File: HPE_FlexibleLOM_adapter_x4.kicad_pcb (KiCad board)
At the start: 4 copper layers, 79.2 x 21.7 mm, 8 parts, among them J1 Connector_PCIe_x8, J2 HPE_FlexibleLOM_x8

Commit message: Add OSHW markings
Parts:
- added H1: MountingHole, Symbol:OSHW-Symbol_6.7x6mm_SilkScreen, F.Cu at (166.6, 114.3)
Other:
- board text added: "Designed by Tobias Schramm"
- board text added: "HPE FlexibleLOM to PCIe adapter"
- board text added: "JLCJLCJLCJLC"
- board text added: "Rev A 2020"
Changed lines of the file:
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@@
   (general
     (thickness 1.6)
-    (drawings 74)
+    (drawings 78)
     (tracks 623)
     (zones 0)
-    (modules 8)
+    (modules 9)
     (nets 81)
   )
@@
     (add_net "Net-(J2-PadB9)")
   )
+  (module Symbol:OSHW-Symbol_6.7x6mm_SilkScreen (layer F.Cu)
+    (at 166.6 114.3)
+    (descr "Open Source Hardware Symbol")
+    (tags "Logo Symbol OSHW")
+    (attr virtual)
+    (fp_text reference H1 (at 0 0) (layer F.SilkS) hide
+      (effects (font (size 1 1) (thickness 0.15)))
+    )
+    (fp_text value MountingHole (at 0.75 0) (layer F.Fab) hide
+      (effects (font (size 1 1) (thickness 0.15)))
+    )
+    (fp_poly (pts (xy 0.555814 -2.531069) (xy 0.639635 -2.086445) (xy 0.94892 -1.958947) (xy 1.258206 -1.831449)
+      (xy 1.629246 -2.083754) (xy 1.733157 -2.154004) (xy 1.827087 -2.216728) (xy 1.906652 -2.269062)
+      (xy 1.96747 -2.308143) (xy 2.005157 -2.331107) (xy 2.015421 -2.336058) (xy 2.03391 -2.323324)
+      (xy 2.07342 -2.288118) (xy 2.129522 -2.234938) (xy 2.197787 -2.168282) (xy 2.273786 -2.092646)
+      (xy 2.353092 -2.012528) (xy 2.431275 -1.932426) (xy 2.503907 -1.856836) (xy 2.566559 -1.790255)
+      (xy 2.614803 -1.737182) (xy 2.64421 -1.702113) (xy 2.651241 -1.690377) (xy 2.641123 -1.66874)
+      (xy 2.612759 -1.621338) (xy 2.569129 -1.552807) (xy 2.513218 -1.467785) (xy 2.448006 -1.370907)
+      (xy 2.410219 -1.31565) (xy 2.341343 -1.214752) (xy 2.28014 -1.123701) (xy 2.229578 -1.04703)
+      (xy 2.192628 -0.989272) (xy 2.172258 -0.954957) (xy 2.169197 -0.947746) (xy 2.176136 -0.927252)
+      (xy 2.195051 -0.879487) (xy 2.223087 -0.811168) (xy 2.257391 -0.729011) (xy 2.295109 -0.63973)
+      (xy 2.333387 -0.550042) (xy 2.36937 -0.466662) (xy 2.400206 -0.396306) (xy 2.423039 -0.34569)
+      (xy 2.435017 -0.321529) (xy 2.435724 -0.320578) (xy 2.454531 -0.315964) (xy 2.504618 -0.305672)
+      (xy 2.580793 -0.290713) (xy 2.677865 -0.272099) (xy 2.790643 -0.250841) (xy 2.856442 -0.238582)
+      (xy 2.97695 -0.215638) (xy 3.085797 -0.193805) (xy 3.177476 -0.174278) (xy 3.246481 -0.158252)
+      (xy 3.287304 -0.146921) (xy 3.295511 -0.143326) (xy 3.303548 -0.118994) (xy 3.310033 -0.064041)
+      (xy 3.31497 0.015108) (xy 3.318364 0.112026) (xy 3.320218 0.220287) (xy 3.320538 0.333465)
+      (xy 3.319327 0.445135) (xy 3.31659 0.548868) (xy 3.312331 0.638241) (xy 3.306555 0.706826)
+      (xy 3.299267 0.748197) (xy 3.294895 0.75681) (xy 3.268764 0.767133) (xy 3.213393 0.781892)
+      (xy 3.136107 0.799352) (xy 3.04423 0.81778) (xy 3.012158 0.823741) (xy 2.857524 0.852066)
+      (xy 2.735375 0.874876) (xy 2.641673 0.89308) (xy 2.572384 0.907583) (xy 2.523471 0.919292)
+      (xy 2.490897 0.929115) (xy 2.470628 0.937956) (xy 2.458626 0.946724) (xy 2.456947 0.948457)
+      (xy 2.440184 0.976371) (xy 2.414614 1.030695) (xy 2.382788 1.104777) (xy 2.34726 1.191965)
+      (xy 2.310583 1.285608) (xy 2.275311 1.379052) (xy 2.243996 1.465647) (xy 2.219193 1.53874)
+      (xy 2.203454 1.591678) (xy 2.199332 1.617811) (xy 2.199676 1.618726) (xy 2.213641 1.640086)
+      (xy 2.245322 1.687084) (xy 2.291391 1.754827) (xy 2.348518 1.838423) (xy 2.413373 1.932982)
+      (xy 2.431843 1.959854) (xy 2.497699 2.057275) (xy 2.55565 2.146163) (xy 2.602538 2.221412)
+      (xy 2.635207 2.27792) (xy 2.6505 2.310581) (xy 2.651241 2.314593) (xy 2.638392 2.335684)
+      (xy 2.602888 2.377464) (xy 2.549293 2.435445) (xy 2.482171 2.505135) (xy 2.406087 2.582045)
+      (xy 2.325604 2.661683) (xy 2.245287 2.739561) (xy 2.169699 2.811186) (xy 2.103405 2.87207)
+      (xy 2.050969 2.917721) (xy 2.016955 2.94365) (xy 2.007545 2.947883) (xy 1.985643 2.937912)
+      (xy 1.9408 2.91102) (xy 1.880321 2.871736) (xy 1.833789 2.840117) (xy 1.749475 2.782098)
+      (xy 1.649626 2.713784) (xy 1.549473 2.645579) (xy 1.495627 2.609075) (xy 1.313371 2.4858)
+      (xy 1.160381 2.56852) (xy 1.090682 2.604759) (xy 1.031414 2.632926) (xy 0.991311 2.648991)
+      (xy 0.981103 2.651226) (xy 0.968829 2.634722) (xy 0.944613 2.588082) (xy 0.910263 2.515609)
+      (xy 0.867588 2.421606) (xy 0.818394 2.310374) (xy 0.76449 2.186215) (xy 0.707684 2.053432)
+      (xy 0.649782 1.916327) (xy 0.592593 1.779202) (xy 0.537924 1.646358) (xy 0.487584 1.522098)
+      (xy 0.44338 1.410725) (xy 0.407119 1.316539) (xy 0.380609 1.243844) (xy 0.365658 1.196941)
+      (xy 0.363254 1.180833) (xy 0.382311 1.160286) (xy 0.424036 1.126933) (xy 0.479706 1.087702)
+      (xy 0.484378 1.084599) (xy 0.628264 0.969423) (xy 0.744283 0.835053) (xy 0.83143 0.685784)
+      (xy 0.888699 0.525913) (xy 0.915086 0.359737) (xy 0.909585 0.191552) (xy 0.87119 0.025655)
+      (xy 0.798895 -0.133658) (xy 0.777626 -0.168513) (xy 0.666996 -0.309263) (xy 0.536302 -0.422286)
+      (xy 0.390064 -0.506997) (xy 0.232808 -0.562806) (xy 0.069057 -0.589126) (xy -0.096667 -0.58537)
+      (xy -0.259838 -0.55095) (xy -0.415935 -0.485277) (xy -0.560433 -0.387765) (xy -0.605131 -0.348187)
+      (xy -0.718888 -0.224297) (xy -0.801782 -0.093876) (xy -0.858644 0.052315) (xy -0.890313 0.197088)
+      (xy -0.898131 0.35986) (xy -0.872062 0.52344) (xy -0.814755 0.682298) (xy -0.728856 0.830906)
+      (xy -0.617014 0.963735) (xy -0.481877 1.075256) (xy -0.464117 1.087011) (xy -0.40785 1.125508)
+      (xy -0.365077 1.158863) (xy -0.344628 1.18016) (xy -0.344331 1.180833) (xy -0.348721 1.203871)
+      (xy -0.366124 1.256157) (xy -0.394732 1.33339) (xy -0.432735 1.431268) (xy -0.478326 1.545491)
+      (xy -0.529697 1.671758) (xy -0.585038 1.805767) (xy -0.642542 1.943218) (xy -0.700399 2.079808)
+      (xy -0.756802 2.211237) (xy -0.809942 2.333205) (xy -0.85801 2.441409) (xy -0.899199 2.531549)
+      (xy -0.931699 2.599323) (xy -0.953703 2.64043) (xy -0.962564 2.651226) (xy -0.98964 2.642819)
+      (xy -1.040303 2.620272) (xy -1.105817 2.587613) (xy -1.141841 2.56852) (xy -1.294832 2.4858)
+      (xy -1.477088 2.609075) (xy -1.570125 2.672228) (xy -1.671985 2.741727) (xy -1.767438 2.807165)
+      (xy -1.81525 2.840117) (xy -1.882495 2.885273) (xy -1.939436 2.921057) (xy -1.978646 2.942938)
+      (xy -1.991381 2.947563) (xy -2.009917 2.935085) (xy -2.050941 2.900252) (xy -2.110475 2.846678)
+      (xy -2.184542 2.777983) (xy -2.269165 2.697781) (xy -2.322685 2.646286) (xy -2.416319 2.554286)
+      (xy -2.497241 2.471999) (xy -2.562177 2.402945) (xy -2.607858 2.350644) (xy -2.631011 2.318616)
+      (xy -2.633232 2.312116) (xy -2.622924 2.287394) (xy -2.594439 2.237405) (xy -2.550937 2.167212)
+      (xy -2.495577 2.081875) (xy -2.43152 1.986456) (xy -2.413303 1.959854) (xy -2.346927 1.863167)
+      (xy -2.287378 1.776117) (xy -2.237984 1.703595) (xy -2.202075 1.650493) (xy -2.182981 1.621703)
+      (xy -2.181136 1.618726) (xy -2.183895 1.595782) (xy -2.198538 1.545336) (xy -2.222513 1.474041)
+      (xy -2.253266 1.388547) (xy -2.288244 1.295507) (xy -2.324893 1.201574) (xy -2.360661 1.113399)
+      (xy -2.392994 1.037634) (xy -2.419338 0.980931) (xy -2.437142 0.949943) (xy -2.438407 0.948457)
+      (xy -2.449294 0.939601) (xy -2.467682 0.930843) (xy -2.497606 0.921277) (xy -2.543103 0.909996)
+      (xy -2.608209 0.896093) (xy -2.696961 0.878663) (xy -2.813393 0.856798) (xy -2.961542 0.829591)
+      (xy -2.993618 0.823741) (xy -3.088686 0.805374) (xy -3.171565 0.787405) (xy -3.23493 0.771569)
+      (xy -3.271458 0.7596) (xy -3.276356 0.75681) (xy -3.284427 0.732072) (xy -3.290987 0.67679)
+      (xy -3.296033 0.597389) (xy -3.299559 0.500296) (xy -3.301561 0.391938) (xy -3.302036 0.27874)
+      (xy -3.300977 0.167128) (xy -3.298382 0.063529) (xy -3.294246 -0.025632) (xy -3.288563 -0.093928)
+      (xy -3.281331 -0.134934) (xy -3.276971 -0.143326) (xy -3.252698 -0.151792) (xy -3.197426 -0.165565)
+      (xy -3.116662 -0.18345) (xy -3.015912 -0.204252) (xy -2.900683 -0.226777) (xy -2.837902 -0.238582)
+      (xy -2.718787 -0.260849) (xy -2.612565 -0.281021) (xy -2.524427 -0.298085) (xy -2.459566 -0.311031)
+      (xy -2.423174 -0.318845) (xy -2.417184 -0.320578) (xy -2.407061 -0.34011) (xy -2.385662 -0.387157)
+      (xy -2.355839 -0.454997) (xy -2.320445 -0.536909) (xy -2.282332 -0.626172) (xy -2.244353 -0.716065)
+      (xy -2.20936 -0.799865) (xy -2.180206 -0.870853) (xy -2.159743 -0.922306) (xy -2.150823 -0.947503)
+      (xy -2.150657 -0.948604) (xy -2.160769 -0.968481) (xy -2.189117 -1.014223) (xy -2.232723 -1.081283)
+      (xy -2.288606 -1.165116) (xy -2.353787 -1.261174) (xy -2.391679 -1.31635) (xy -2.460725 -1.417519)
+      (xy -2.52205 -1.50937) (xy -2.572663 -1.587256) (xy -2.609571 -1.646531) (xy -2.629782 -1.682549)
+      (xy -2.632701 -1.690623) (xy -2.620153 -1.709416) (xy -2.585463 -1.749543) (xy -2.533063 -1.806507)
+      (xy -2.467384 -1.875815) (xy -2.392856 -1.952969) (xy -2.313913 -2.033475) (xy -2.234983 -2.112837)
+      (xy -2.1605 -2.18656) (xy -2.094894 -2.250148) (xy -2.042596 -2.299106) (xy -2.008039 -2.328939)
+      (xy -1.996478 -2.336058) (xy -1.977654 -2.326047) (xy -1.932631 -2.297922) (xy -1.865787 -2.254546)
+      (xy -1.781499 -2.198782) (xy -1.684144 -2.133494) (xy -1.610707 -2.083754) (xy -1.239667 -1.831449)
+      (xy -0.621095 -2.086445) (xy -0.537275 -2.531069) (xy -0.453454 -2.975693) (xy 0.471994 -2.975693)
+      (xy 0.555814 -2.531069)) (layer F.SilkS) (width 0.01))
+  )
   (module Jumper:SolderJumper-3_P1.3mm_Bridged12_Pad1.0x1.5mm (layer F.Cu)
     (at 104.75 109.75)
@@
       (net 78 GND))
   )
+  (gr_text JLCJLCJLCJLC (at 96.8 103.45 45) (layer F.SilkS)
+    (effects (font (size 0.8 0.8) (thickness 0.15)))
+  )
+  (gr_text "Rev A 2020" (at 126.7 115.55) (layer F.SilkS)
+    (effects (font (size 1.5 1.5) (thickness 0.25)))
+  )
+  (gr_text "Designed by Tobias Schramm" (at 136.85 112.5) (layer F.SilkS)
+    (effects (font (size 1.5 1.5) (thickness 0.25)))
+  )
+  (gr_text "HPE FlexibleLOM to PCIe adapter" (at 139.05 109.5) (layer F.SilkS)
+    (effects (font (size 1.5 1.5) (thickness 0.25)))
+  )
   (gr_text lanes (at 105 112) (layer F.SilkS)

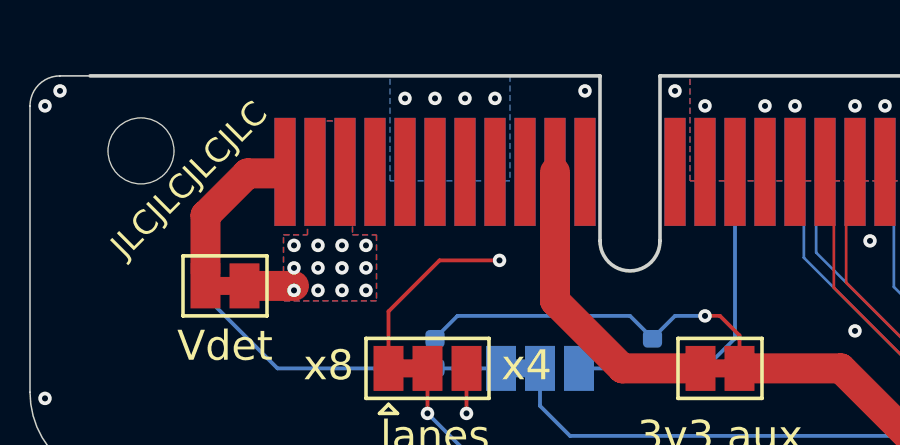
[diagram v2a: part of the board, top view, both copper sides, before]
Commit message: Reverse engineer some more FlexibleLOM signals
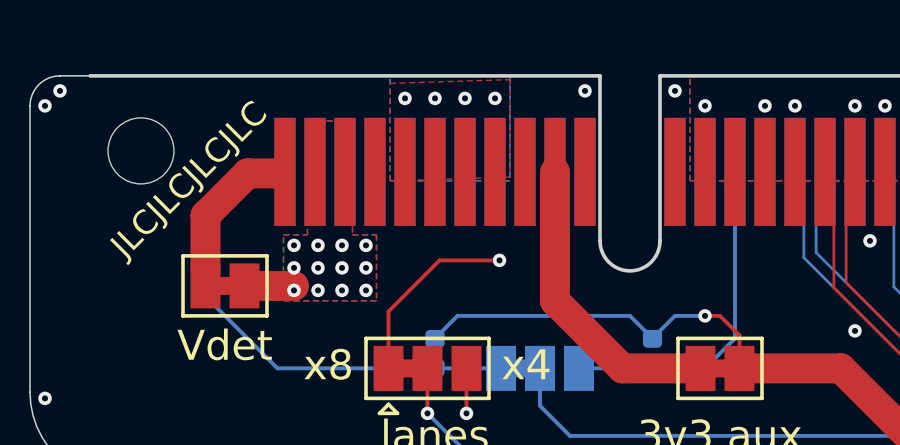
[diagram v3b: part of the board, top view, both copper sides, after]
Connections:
- J2 pad B6: Net-(J2-PadB6) -> GND
